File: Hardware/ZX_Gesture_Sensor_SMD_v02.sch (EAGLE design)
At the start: 50 parts, among them Q1 MMBT2222A, Q2 MOSFET-NCHANNEL2N7002PW, U1 PIC16F1823-14PINTSSOP, U2 MCP6021T-E/OT, U3 DMC2700UDM, U4 DMC2700UDM, U6 TSOP57238TT1

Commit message: Updated Board and Schematic Files
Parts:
- JP3: value (none) -> Note: use 1x3 male headers (CONN-009692)
- U6: PLACE DNP -> (none)
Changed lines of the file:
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@@
 <part name="U3" library="SparkFun-DiscreteSemi" deviceset="DMC2700UDM" device=""/>
 <part name="U4" library="SparkFun-DiscreteSemi" deviceset="DMC2700UDM" device=""/>
-<part name="U6" library="SparkFun-Sensors" deviceset="TSOP57238TT1" device="">
-<attribute name="PLACE" value="DNP"/>
-</part>
+<part name="U6" library="SparkFun-Sensors" deviceset="TSOP57238TT1" device=""/>
 <part name="JP1" library="SparkFun-Connectors" deviceset="M06" device="NO_SILK_FEMALE_PTH"/>
-<part name="JP3" library="SparkFun-Connectors" deviceset="M03" device="1X03_NO_SILK"/>
+<part name="JP3" library="SparkFun-Connectors" deviceset="M03" device="1X03_NO_SILK" value="Note: use 1x3 male headers (CONN-009692)"/>
 <part name="GND1" library="SparkFun-Aesthetics" deviceset="GND" device=""/>
 <part name="SUPPLY1" library="SparkFun-Aesthetics" deviceset="VCC" device=""/>
@@
 <instance part="U3" gate="G$1" x="22.86" y="111.76"/>
 <instance part="U4" gate="G$1" x="88.9" y="111.76"/>
-<instance part="U6" gate="G$1" x="198.12" y="63.5" smashed="yes">
-<attribute name="NAME" x="187.96" y="69.342" size="1.778" layer="95"/>
-<attribute name="VALUE" x="187.706" y="56.388" size="1.778" layer="96"/>
-</instance>
+<instance part="U6" gate="G$1" x="198.12" y="63.5"/>
 <instance part="JP1" gate="G$1" x="12.7" y="154.94" smashed="yes">
 <attribute name="VALUE" x="7.62" y="144.78" size="1.778" layer="96"/>

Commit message: Updated Board and schematic files
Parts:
- removed D4: SFH4641SHORT2, SparkFun-LED:SFH4641SHORT2
- added D2: SFH4641SHORT2, SparkFun-LED:SFH4641SHORT2
- renumbered D3 to D1
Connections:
- net COMMON: now also D2.C; no longer D4.C
- net N$12: now also D2.A; no longer D4.A
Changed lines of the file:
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@@
 <part name="TP5" library="SparkFun-Passives" deviceset="TEST-POINT" device="3X4" value="TEST-POINT3X4"/>
 <part name="U$6" library="SparkFun-Aesthetics" deviceset="GESTURESENSE_LOGOS" device="TEXT"/>
-<part name="D3" library="SparkFun-LED" deviceset="SFH4641" device="SHORT2"/>
-<part name="D4" library="SparkFun-LED" deviceset="SFH4641" device="SHORT2"/>
+<part name="D1" library="SparkFun-LED" deviceset="SFH4641" device="SHORT2"/>
+<part name="D2" library="SparkFun-LED" deviceset="SFH4641" device="SHORT2"/>
 <part name="R14" library="SparkFun-Resistors" deviceset="1KOHM-1/10W-1%(0603)" device="" value="1K"/>
 <part name="FID4" library="SparkFun-Aesthetics" deviceset="FIDUCIAL" device="UFIDUCIAL" value="FIDUCIALUFIDUCIAL"/>
@@
 </instance>
 <instance part="U$6" gate="G$1" x="111.76" y="2.54"/>
-<instance part="D3" gate="G$1" x="48.26" y="104.14" smashed="yes">
+<instance part="D1" gate="G$1" x="48.26" y="104.14" smashed="yes">
 <attribute name="NAME" x="49.53" y="107.188" size="1.778" layer="95"/>
 <attribute name="VALUE" x="49.276" y="98.806" size="1.778" layer="96"/>
 </instance>
-<instance part="D4" gate="G$1" x="114.3" y="106.68" smashed="yes">
-<attribute name="NAME" x="115.57" y="109.728" size="1.778" layer="95"/>
-<attribute name="VALUE" x="115.316" y="101.346" size="1.778" layer="96"/>
+<instance part="D2" gate="G$1" x="114.3" y="104.14" smashed="yes">
+<attribute name="NAME" x="115.57" y="107.188" size="1.778" layer="95"/>
+<attribute name="VALUE" x="115.316" y="98.806" size="1.778" layer="96"/>
 </instance>
 <instance part="R14" gate="G$1" x="73.66" y="119.38" rot="R90"/>
@@
 <wire x1="48.26" y1="78.74" x2="50.8" y2="78.74" width="0.1524" layer="91"/>
 <junction x="48.26" y="78.74"/>
-<pinref part="D3" gate="G$1" pin="C"/>
+<pinref part="D1" gate="G$1" pin="C"/>
 <wire x1="48.26" y1="99.06" x2="48.26" y2="78.74" width="0.1524" layer="91"/>
 </segment>
@@
 <wire x1="116.84" y1="78.74" x2="114.3" y2="78.74" width="0.1524" layer="91"/>
 <junction x="114.3" y="78.74"/>
-<pinref part="D4" gate="G$1" pin="C"/>
-<wire x1="114.3" y1="101.6" x2="114.3" y2="78.74" width="0.1524" layer="91"/>
+<pinref part="D2" gate="G$1" pin="C"/>
+<wire x1="114.3" y1="99.06" x2="114.3" y2="78.74" width="0.1524" layer="91"/>
 </segment>
 </net>
@@
 <segment>
 <pinref part="R6" gate="G$1" pin="2"/>
-<pinref part="D3" gate="G$1" pin="A"/>
+<pinref part="D1" gate="G$1" pin="A"/>
 <wire x1="45.72" y1="109.22" x2="48.26" y2="109.22" width="0.1524" layer="91"/>
 <wire x1="48.26" y1="109.22" x2="48.26" y2="106.68" width="0.1524" layer="91"/>
@@
 <segment>
 <pinref part="R14" gate="G$1" pin="2"/>
-<wire x1="73.66" y1="124.46" x2="73.66" y2="127" width="0.2032" layer="91"/>
+<wire x1="73.66" y1="124.46" x2="73.66" y2="127" width="0.1524" layer="91"/>
 <label x="73.66" y="127" size="1.27" layer="95" xref="yes"/>
 </segment>
@@
 </segment>
 </net>
-<net name="N$12" class="0">
-<segment>
-<pinref part="R8" gate="G$1" pin="2"/>
-<pinref part="D4" gate="G$1" pin="A"/>
-<wire x1="111.76" y1="109.22" x2="114.3" y2="109.22" width="0.1524" layer="91"/>
-</segment>
-</net>
 <net name="RECEIVER" class="0">
 <segment>
@@
 <pinref part="R14" gate="G$1" pin="1"/>
 <pinref part="U4" gate="G$1" pin="G1"/>
-<wire x1="73.66" y1="114.3" x2="78.74" y2="114.3" width="0.2032" layer="91"/>
+<wire x1="73.66" y1="114.3" x2="78.74" y2="114.3" width="0.1524" layer="91"/>
 </segment>
 </net>
@@
 </segment>
 </net>
+<net name="N$12" class="0">
+<segment>
+<pinref part="D2" gate="G$1" pin="A"/>
+<wire x1="114.3" y1="106.68" x2="114.3" y2="109.22" width="0.1524" layer="91"/>
+<pinref part="R8" gate="G$1" pin="2"/>
+<wire x1="114.3" y1="109.22" x2="111.76" y2="109.22" width="0.1524" layer="91"/>
+</segment>
+</net>

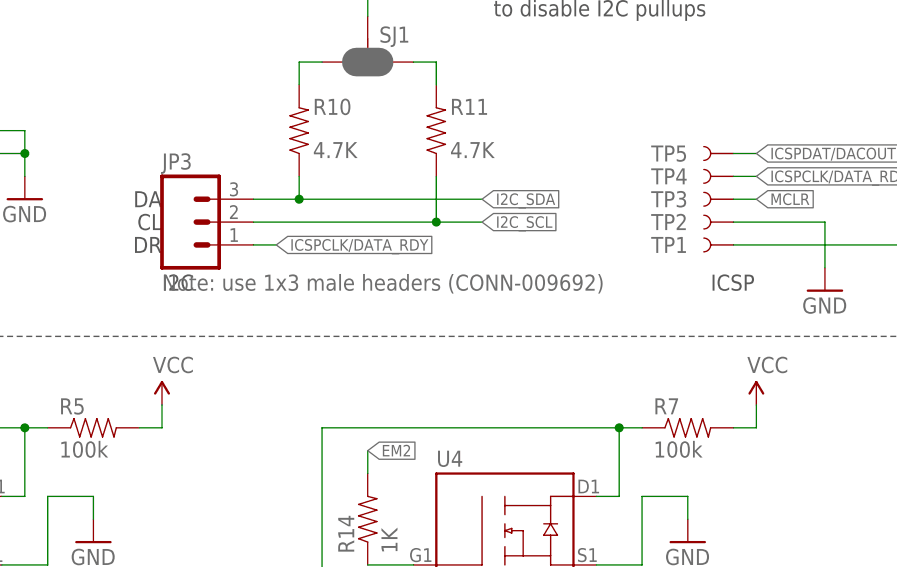
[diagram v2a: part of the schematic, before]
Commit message: Updated Board and Schematic per QC
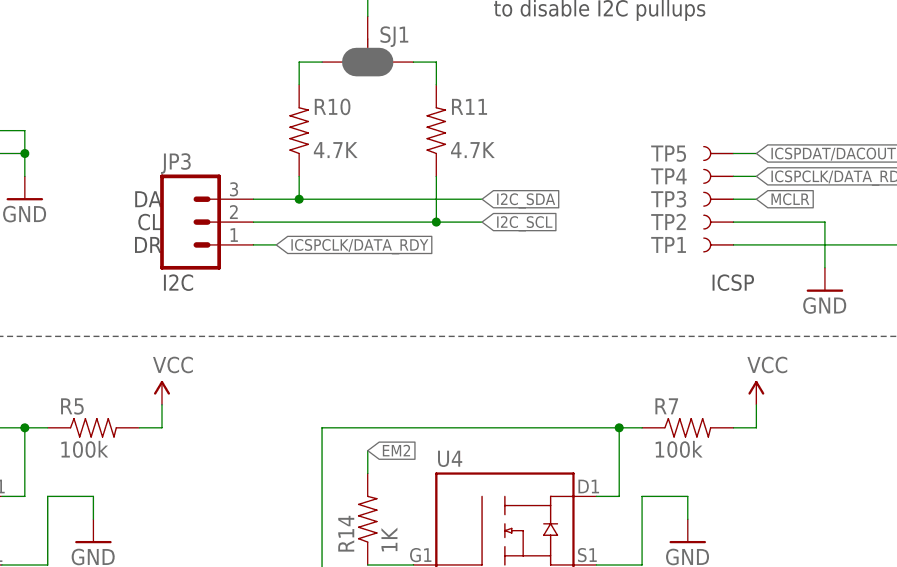
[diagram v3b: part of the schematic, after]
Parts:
- JP3: value Note: use 1x3 male headers (CONN-009692) -> (none)
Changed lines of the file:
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@@
 <part name="U6" library="SparkFun-Sensors" deviceset="TSOP57238TT1" device=""/>
 <part name="JP1" library="SparkFun-Connectors" deviceset="M06" device="NO_SILK_FEMALE_PTH"/>
-<part name="JP3" library="SparkFun-Connectors" deviceset="M03" device="1X03_NO_SILK" value="Note: use 1x3 male headers (CONN-009692)"/>
+<part name="JP3" library="SparkFun-Connectors" deviceset="M03" device="1X03_NO_SILK"/>
 <part name="GND1" library="SparkFun-Aesthetics" deviceset="GND" device=""/>
 <part name="SUPPLY1" library="SparkFun-Aesthetics" deviceset="VCC" device=""/>

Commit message: Updated Sch
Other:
- note removed: "DNP"
- moved on the sheet: R13
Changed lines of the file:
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@@
 <text x="50.8" y="149.86" size="1.778" layer="97" align="center-right">DR</text>
 <text x="7.62" y="149.86" size="1.778" layer="97" align="center-right">NC</text>
-<text x="59.69" y="104.902" size="1.778" layer="97">DNP</text>
-<text x="125.73" y="104.902" size="1.778" layer="97">DNP</text>
 <text x="7.62" y="177.8" size="1.778" layer="97">NOTE: VCC must be 3.3V - 5V</text>
 <text x="172.212" y="11.684" size="1.778" layer="94" font="vector">Shawn Hymel </text>
@@
 <instance part="R14" gate="G$1" x="73.66" y="119.38" rot="R90"/>
 <instance part="FID4" gate="G$1" x="236.22" y="33.02"/>
-<instance part="R13" gate="G$1" x="7.62" y="121.92" rot="R90"/>
+<instance part="R13" gate="G$1" x="7.62" y="119.38" rot="R90"/>
 <instance part="FRAME1" gate="G$1" x="0" y="0"/>
 <instance part="FRAME1" gate="V" x="147.32" y="0"/>
@@
 <segment>
 <pinref part="R13" gate="G$1" pin="2"/>
-<wire x1="7.62" y1="127" x2="10.16" y2="127" width="0.1524" layer="91"/>
-<label x="10.16" y="127" size="1.27" layer="95" xref="yes"/>
+<wire x1="7.62" y1="124.46" x2="7.62" y2="127" width="0.1524" layer="91"/>
+<label x="7.62" y="127" size="1.27" layer="95" xref="yes"/>
 </segment>
 </net>
@@
 <segment>
 <pinref part="R13" gate="G$1" pin="1"/>
-<wire x1="7.62" y1="116.84" x2="7.62" y2="114.3" width="0.1524" layer="91"/>
 <pinref part="U3" gate="G$1" pin="G1"/>
 <wire x1="7.62" y1="114.3" x2="12.7" y2="114.3" width="0.1524" layer="91"/>
